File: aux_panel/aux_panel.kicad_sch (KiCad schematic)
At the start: 5 parts

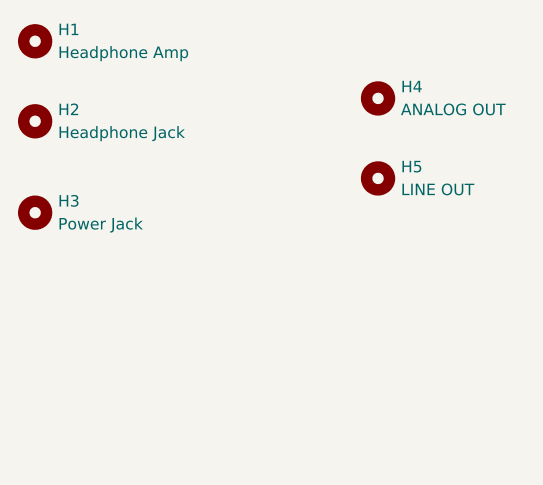
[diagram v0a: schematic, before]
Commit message: Complete aux panel PCB
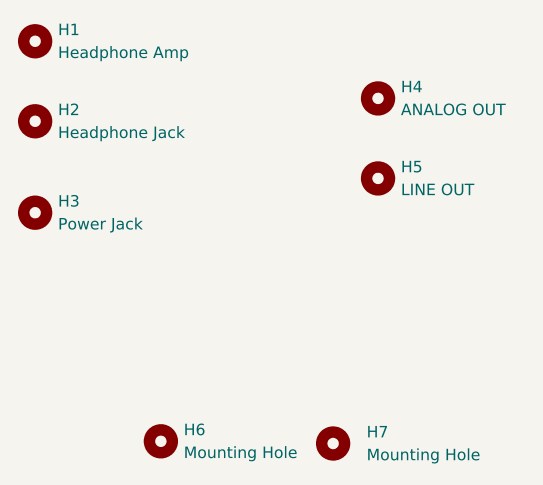
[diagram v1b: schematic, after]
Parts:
- added H6, H7: Mounting Hole, MountingHole:MountingHole_3.2mm_M3, symbol Mechanical:MountingHole
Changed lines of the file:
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@@
+    )
+  )
+  (symbol (lib_id "Mechanical:MountingHole") (at 138.43 127 0) (unit 1)
+    (in_bom yes) (on_board yes) (fields_autoplaced)
+    (property "Reference" "H6" (id 0) (at 140.97 125.7299 0)
+      (effects (font (size 1.27 1.27)) (justify left))
+    )
+    (property "Value" "Mounting Hole" (id 1) (at 140.97 128.2699 0)
+      (effects (font (size 1.27 1.27)) (justify left))
+    )
+    (property "Footprint" "MountingHole:MountingHole_3.2mm_M3" (id 2) (at 138.43 127 0)
+      (effects (font (size 1.27 1.27)) hide)
+    )
+    (property "Datasheet" "~" (id 3) (at 138.43 127 0)
+      (effects (font (size 1.27 1.27)) hide)
+    )
+  )
+  (symbol (lib_id "Mechanical:MountingHole") (at 157.5686 127.2447 0) (unit 1)
+    (in_bom yes) (on_board yes) (fields_autoplaced)
+    (property "Reference" "H7" (id 0) (at 161.29 125.9746 0)
+      (effects (font (size 1.27 1.27)) (justify left))
+    )
+    (property "Value" "Mounting Hole" (id 1) (at 161.29 128.5146 0)
+      (effects (font (size 1.27 1.27)) (justify left))
+    )
+    (property "Footprint" "MountingHole:MountingHole_3.2mm_M3" (id 2) (at 157.5686 127.2447 0)
+      (effects (font (size 1.27 1.27)) hide)
+    )
+    (property "Datasheet" "~" (id 3) (at 157.5686 127.2447 0)
+      (effects (font (size 1.27 1.27)) hide)
     )
   )
@@
       (reference "H5") (unit 1) (value "LINE OUT") (footprint "kosmo-lib:Hole_Jack")
     )
+    (path "/ade7341f-0c5a-4543-a727-bbebc0353a87"
+      (reference "H6") (unit 1) (value "Mounting Hole") (footprint "MountingHole:MountingHole_3.2mm_M3")
+    )
+    (path "/c4893d8a-4904-4d8e-ae73-3a8980341a7b"
+      (reference "H7") (unit 1) (value "Mounting Hole") (footprint "MountingHole:MountingHole_3.2mm_M3")
+    )
   )
